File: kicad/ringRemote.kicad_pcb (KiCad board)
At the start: 4 copper layers, 13.2 x 13.8 mm, 23 parts, among them Y1 32.768kHz

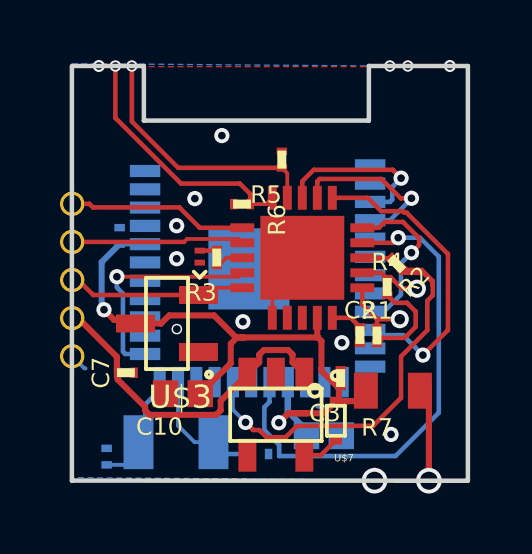
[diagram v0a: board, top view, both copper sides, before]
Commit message: moved code into a sub dir and added an eclipse workspace to save debug config; fixed compile errors
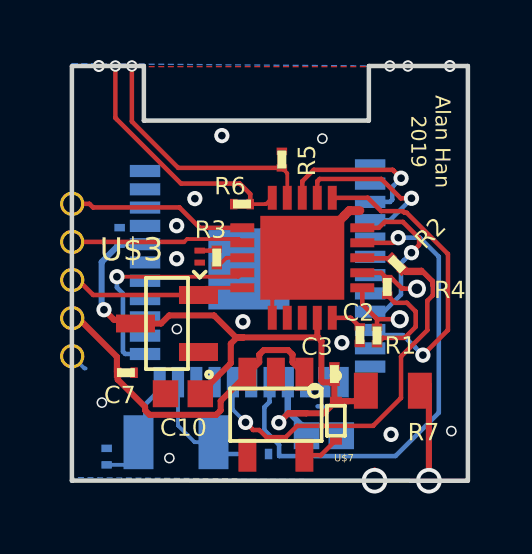
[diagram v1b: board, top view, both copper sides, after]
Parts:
- moved C3 0.25 mm to (151.2, 103.8)
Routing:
- net GND: track 9.28 -> 11.9 mm, vias 9 -> 13
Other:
- board text added: "2019.01.25"
- board text added: "Alan Han 2019"
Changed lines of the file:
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@@
   (general
     (thickness 1.6)
-    (drawings 8)
-    (tracks 287)
+    (drawings 10)
+    (tracks 296)
     (zones 0)
     (modules 23)
@@
     (at 152.0011 102.4536)
     (descr "Perfect 0201 for Reflow Soldering\n<p>0.024\" L x 0.012\" W (0.60mm x 0.30mm)")
-    (fp_text reference C2 (at 0 -0.83) (layer F.SilkS)
+    (fp_text reference C2 (at -0.0511 -0.7536) (layer F.SilkS)
       (effects (font (size 0.57912 0.57912) (thickness 0.09144)))
     )
@@
   )
   (module ringRemote:0201 (layer Top)
-    (at 151.3611 103.8836 180)
-    (descr "Perfect 0201 for Reflow Soldering\n<p>0.024\" L x 0.012\" W (0.60mm x 0.30mm)")
-    (fp_text reference C3 (at 0 -0.83 180) (layer F.SilkS)
+    (at 151.15 103.75 180)
+    (descr "Perfect 0201 for Reflow Soldering\n<p>0.024\" L x 0.012\" W (0.60mm x 0.30mm)")
+    (fp_text reference C3 (at 0.05 1.25 180) (layer F.SilkS)
       (effects (font (size 0.57912 0.57912) (thickness 0.09144)) (justify right top))
     )
@@
     (at 153.2311 100.0836 225)
     (descr "Perfect 0201 for Reflow Soldering\n<p>0.024\" L x 0.012\" W (0.60mm x 0.30mm)")
-    (fp_text reference R2 (at 0 -0.830001 225) (layer F.SilkS)
+    (fp_text reference R2 (at -1.522047 -0.060316 45) (layer F.SilkS)
       (effects (font (size 0.57912 0.57912) (thickness 0.09144)))
     )
@@
       (effects (font (size 0.57912 0.57912) (thickness 0.12192)) (justify top mirror))
     )
-    (fp_text user >Name (at 0 1.043 180) (layer B.SilkS)
+    (fp_text user Y1 (at 1.67 1.22 180) (layer B.SilkS)
       (effects (font (size 0.57912 0.57912) (thickness 0.12192)) (justify bottom mirror))
     )
@@
     (at 143.9911 99.1436)
     (descr "Perfect 0201 for Reflow Soldering\n<p>0.024\" L x 0.012\" W (0.60mm x 0.30mm)")
-    (fp_text reference C4 (at 0 0.83) (layer B.SilkS)
+    (fp_text reference C4 (at -0.3911 -0.7936) (layer B.SilkS)
       (effects (font (size 0.57912 0.57912) (thickness 0.09144)) (justify mirror))
     )
@@
     (at 143.56 106.5)
     (descr "Perfect 0201 for Reflow Soldering\n<p>0.024\" L x 0.012\" W (0.60mm x 0.30mm)")
-    (fp_text reference C5 (at 0 0.83) (layer B.SilkS)
+    (fp_text reference C5 (at -0.16 -1.05) (layer B.SilkS)
       (effects (font (size 0.57912 0.57912) (thickness 0.09144)) (justify mirror))
     )
@@
     (at 147.2311 99.8636 180)
     (descr "Perfect 0201 for Reflow Soldering\n<p>0.024\" L x 0.012\" W (0.60mm x 0.30mm)")
-    (fp_text reference R3 (at 0 -0.83 180) (layer F.SilkS)
+    (fp_text reference R3 (at -0.3189 1.2636 180) (layer F.SilkS)
       (effects (font (size 0.57912 0.57912) (thickness 0.09144)) (justify right top))
     )
@@
     (at 152.5711 102.4636)
     (descr "Perfect 0201 for Reflow Soldering\n<p>0.024\" L x 0.012\" W (0.60mm x 0.30mm)")
-    (fp_text reference R1 (at 0 -0.83) (layer F.SilkS)
+    (fp_text reference R1 (at 0.7789 0.3364) (layer F.SilkS)
       (effects (font (size 0.57912 0.57912) (thickness 0.09144)))
     )
@@
     (at 152.9111 100.8436)
     (descr "Perfect 0201 for Reflow Soldering\n<p>0.024\" L x 0.012\" W (0.60mm x 0.30mm)")
-    (fp_text reference R4 (at 0 -0.83) (layer F.SilkS)
+    (fp_text reference R4 (at 2.0889 0.1064) (layer F.SilkS)
       (effects (font (size 0.57912 0.57912) (thickness 0.09144)))
     )
@@
     (at 149.4 96.6 180)
     (descr "Perfect 0201 for Reflow Soldering\n<p>0.024\" L x 0.012\" W (0.60mm x 0.30mm)")
-    (fp_text reference R5 (at 0 -0.83 180) (layer F.SilkS)
+    (fp_text reference R5 (at -0.5 0.5 270) (layer F.SilkS)
       (effects (font (size 0.57912 0.57912) (thickness 0.09144)) (justify right top))
     )
@@
     (at 148.0711 98.0836 270)
     (descr "Perfect 0201 for Reflow Soldering\n<p>0.024\" L x 0.012\" W (0.60mm x 0.30mm)")
-    (fp_text reference R6 (at 0 -0.83 270) (layer F.SilkS)
+    (fp_text reference R6 (at -0.9336 -0.1289) (layer F.SilkS)
       (effects (font (size 0.57912 0.57912) (thickness 0.09144)) (justify right top))
     )
@@
   (module ringRemote:3-SOT-23 (layer Top)
     (at 145.5711 102.0636 180)
-    (fp_text reference U$3 (at -1.5 -2 180) (layer F.SilkS)
+    (fp_text reference U$3 (at 0.1211 2.9136) (layer F.SilkS)
       (effects (font (size 0.77216 0.77216) (thickness 0.065024)) (justify right top))
     )
@@
     (at 153.1011 104.3036 180)
     (descr "<p><b>Generic 2012 (0805) package</b></p>\n<p>0.2mm courtyard excess rounded to nearest 0.05mm.</p>")
-    (fp_text reference R7 (at 0 -0.889 180) (layer F.SilkS)
+    (fp_text reference R7 (at -1.5489 -1.0464 180) (layer F.SilkS)
       (effects (font (size 0.57912 0.57912) (thickness 0.12192)) (justify right top))
     )
@@
     (at 144.2011 103.7036 90)
     (descr "Perfect 0201 for Reflow Soldering\n<p>0.024\" L x 0.012\" W (0.60mm x 0.30mm)")
-    (fp_text reference C7 (at 0 -0.83 90) (layer F.SilkS)
+    (fp_text reference C7 (at -0.7464 -0.2011 180) (layer F.SilkS)
       (effects (font (size 0.57912 0.57912) (thickness 0.09144)))
     )
@@
     (at 150.8011 105.8036)
     (descr "<p><b>Generic 1005 (0402) package</b></p>\n<p>0.2mm courtyard excess rounded to nearest 0.05mm.</p>")
-    (fp_text reference C9 (at 0 0.762) (layer B.SilkS)
+    (fp_text reference C9 (at -0.0511 1.1464) (layer B.SilkS)
       (effects (font (size 0.57912 0.57912) (thickness 0.12192)) (justify bottom mirror))
     )
@@
     (at 146.1011 104.4036 180)
     (descr "<p><b>Generic 1005 (0402) package</b></p>\n<p>0.2mm courtyard excess rounded to nearest 0.05mm.</p>")
-    (fp_text reference C10 (at 0 -0.762 180) (layer F.SilkS)
+    (fp_text reference C10 (at -0.7989 -0.7964 180) (layer F.SilkS)
       (effects (font (size 0.57912 0.57912) (thickness 0.12192)) (justify right top))
     )
@@
     (pad 1 smd rect (at -0.58 0 180) (size 0.85 0.9) (layers Top F.Paste F.Mask)
       (net 2 VCC) (solder_mask_margin 0.0635))
+  )
+  (gr_text 2019.01.25 (at 154.8 96.35 270) (layer B.SilkS)
+    (effects (font (size 0.5 0.5) (thickness 0.125)) (justify mirror))
+  )
+  (gr_text "Alan Han \n2019" (at 154.35 96 270) (layer F.SilkS)
+    (effects (font (size 0.5 0.5) (thickness 0.125)))
   )
   (gr_line (start 152.3 93.48) (end 155.601 93.48) (layer Edge.Cuts) (width 0.15))
@@
   (segment (start 149.0811 100.8736) (end 150.0811 99.8736) (width 0.127) (layer Top) (net 1))
   (segment (start 149.0811 101.8736) (end 149.0811 100.8736) (width 0.127) (layer Top) (net 1))
+  (segment (start 150.0811 99.8736) (end 151.483501 98.471199) (width 0.3) (layer Top) (net 1))
+  (segment (start 151.483501 98.471199) (end 151.483501 98.466499) (width 0.3) (layer Top) (net 1))
+  (segment (start 151.483501 98.466499) (end 151.65 98.3) (width 0.3) (layer Top) (net 1))
+  (segment (start 151.65 98.3) (end 152 98.3) (width 0.3) (layer Top) (net 1))
+  (via (at 150.75 95.9) (size 0.3556) (drill 0.254) (layers Top Bottom) (net 1))
+  (via (at 143.4 104.7) (size 0.3556) (drill 0.254) (layers Top Bottom) (net 1))
+  (via (at 145.65 106.55) (size 0.3556) (drill 0.254) (layers Top Bottom) (net 1))
+  (via (at 155.05 105.65) (size 0.3556) (drill 0.254) (layers Top Bottom) (net 1))
   (via (at 149.299081 105.37) (size 0.508) (drill 0.254) (layers Top Bottom) (net 2))
   (segment (start 151.2011 104.6536) (end 151.3011 104.6536) (width 0.2032) (layer Top) (net 2))
@@
   (segment (start 152.0011 104.3956) (end 152.3011 104.0956) (width 0.2032) (layer Top) (net 2))
   (segment (start 152.3011 104.0956) (end 152.2011 104.3036) (width 0.2032) (layer Top) (net 2))
-  (segment (start 151.3611 104.1586) (end 151.3011 104.2186) (width 0.2032) (layer Top) (net 2))
-  (segment (start 151.3011 104.2186) (end 151.3011 104.6536) (width 0.2032) (layer Top) (net 2))
-  (segment (start 150.7201 103.6376) (end 151.3011 104.2186) (width 0.2032) (layer Top) (net 2))
   (segment (start 151.2011 104.6536) (end 150.7987 105.056) (width 0.2032) (layer Top) (net 2))
   (segment (start 144.5211 102.0636) (end 144.6411 101.9436) (width 0.2032) (layer Top) (net 2))
@@
   (segment (start 150.6 102.5276) (end 150.5811 102.5087) (width 0.2032) (layer Top) (net 2))
   (segment (start 148.12 102.5276) (end 150.6 102.5276) (width 0.2032) (layer Top) (net 2))
-  (segment (start 150.7201 102.6477) (end 150.7201 103.6376) (width 0.2032) (layer Top) (net 2))
+  (segment (start 150.7718 104.025) (end 151.15 104.025) (width 0.2032) (layer Top) (net 2))
+  (segment (start 150.7201 103.9733) (end 150.7718 104.025) (width 0.2032) (layer Top) (net 2))
+  (segment (start 150.7201 102.6477) (end 150.7201 103.9733) (width 0.2032) (layer Top) (net 2))
   (segment (start 150.6 102.5276) (end 150.7201 102.6477) (width 0.2032) (layer Top) (net 2))
+  (segment (start 151.15 104.6025) (end 151.2011 104.6536) (width 0.2032) (layer Top) (net 2))
+  (segment (start 151.15 104.025) (end 151.15 104.6025) (width 0.2032) (layer Top) (net 2))
   (segment (start 144.8511 106.0236) (end 144.8511 104.7536) (width 0.1524) (layer Bottom) (net 3))
   (segment (start 145.3286 104.2761) (end 145.3286 104.0191) (width 0.1524) (layer Bottom) (net 3))
